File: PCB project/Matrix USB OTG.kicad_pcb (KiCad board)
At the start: 2 copper layers, 27.5 x 20.2 mm, 2 parts, among them J1 USB3150-30-130-A, J2 SSM-102-L-DV

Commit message: Final schematic and initial constraints
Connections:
- J2 pad 01: /USB_DN -> /USB_DP
- J2 pad 02: VBUS -> /USB_DN
- J2 pad 03: /USB_DP -> GND
- J2 pad 04: GND -> VBUS
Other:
- board size 27.5 x 20.2 mm -> 29.2 x 19.5 mm
- board text added: "DN"
- board text added: "DP"
- board text added: "GND"
- board text added: "VBUS"
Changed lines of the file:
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@@
 	)
 	(setup
+		(stackup
+			(layer "F.SilkS"
+				(type "Top Silk Screen")
+			)
+			(layer "F.Paste"
+				(type "Top Solder Paste")
+			)
+			(layer "F.Mask"
+				(type "Top Solder Mask")
+				(thickness 0.01)
+			)
+			(layer "F.Cu"
+				(type "copper")
+				(thickness 0.035)
+			)
+			(layer "dielectric 1"
+				(type "core")
+				(thickness 1.51)
+				(material "FR4")
+				(epsilon_r 4.5)
+				(loss_tangent 0.02)
+			)
+			(layer "B.Cu"
+				(type "copper")
+				(thickness 0.035)
+			)
+			(layer "B.Mask"
+				(type "Bottom Solder Mask")
+				(thickness 0.01)
+			)
+			(layer "B.Paste"
+				(type "Bottom Solder Paste")
+			)
+			(layer "B.SilkS"
+				(type "Bottom Silk Screen")
+			)
+			(copper_finish "None")
+			(dielectric_constraints no)
+		)
 		(pad_to_mask_clearance 0)
 		(allow_soldermask_bridges_in_footprints no)
@@
 		(capping no)
 		(filling no)
+		(zone_defaults)
 		(pcbplotparams
 			(layerselection 0x00000000_00000000_55555555_5755f5ff)
@@
 		(at 107.75 98.5 90)
 		(property "Reference" "J2"
-			(at -0.365 -5.82 90)
+			(at 1.75 8.5 180)
 			(layer "F.SilkS")
 			(effects
@@
 			(size 1.02 2.22)
 			(layers "F.Cu" "F.Mask" "F.Paste")
-			(net "/USB_DN")
+			(net "/USB_DP")
 			(pinfunction "01_01")
 			(pintype "passive")
@@
 			(size 1.02 2.22)
 			(layers "F.Cu" "F.Mask" "F.Paste")
-			(net "VBUS")
+			(net "/USB_DN")
 			(pinfunction "02_02")
 			(pintype "passive")
@@
 			(size 1.02 2.22)
 			(layers "F.Cu" "F.Mask" "F.Paste")
-			(net "/USB_DP")
+			(net "GND")
 			(pinfunction "03_03")
 			(pintype "passive")
@@
 			(size 1.02 2.22)
 			(layers "F.Cu" "F.Mask" "F.Paste")
-			(net "GND")
+			(net "VBUS")
 			(pinfunction "04_04")
 			(pintype "passive")
@@
 		(pad "1" thru_hole circle
 			(at 0 0 180)
-			(size 0.8128 0.8128)
+			(size 0.7628 0.7128)
 			(drill 0.4572)
 			(layers "*.Cu" "*.Mask")
@@
 		(pad "2" thru_hole circle
 			(at 0.650001 0.65 180)
-			(size 0.8128 0.8128)
+			(size 0.7628 0.7628)
 			(drill 0.4572)
 			(layers "*.Cu" "*.Mask")
@@
 		(pad "3" thru_hole circle
 			(at 1.3 0 180)
-			(size 0.8128 0.8128)
+			(size 0.7628 0.7628)
 			(drill 0.4572)
 			(layers "*.Cu" "*.Mask")
@@
 		(pad "4" thru_hole circle
 			(at 1.949999 0.65 180)
-			(size 0.8128 0.8128)
+			(size 0.7628 0.7128)
 			(drill 0.4572)
 			(layers "*.Cu" "*.Mask")
@@
 		(pad "5" thru_hole circle
 			(at 2.6 0 180)
-			(size 0.8128 0.8128)
+			(size 0.7628 0.7128)
 			(drill 0.4572)
 			(layers "*.Cu" "*.Mask")
@@
 		(pad "6" thru_hole circle
 			(at -0.2 1.580001 180)
-			(size 0.8636 0.8636)
+			(size 0.7636 0.7636)
 			(drill 0.5588)
 			(layers "*.Cu" "*.Mask")
@@
 		(pad "7" thru_hole circle
 			(at 2.799999 1.580001 180)
-			(size 0.8636 0.8636)
+			(size 0.7636 0.7636)
 			(drill 0.5588)
 			(layers "*.Cu" "*.Mask")
@@
 		(pad "8" thru_hole circle
 			(at -0.2 -0.919999 180)
-			(size 0.8636 0.8636)
+			(size 0.7636 0.7636)
 			(drill 0.5588)
 			(layers "*.Cu" "*.Mask")
@@
 			(pinfunction "GND_8")
 			(pintype "power_in")
+			(clearance 0)
 		)
 		(pad "9" thru_hole circle
 			(at 2.799999 -0.919999 180)
-			(size 0.8636 0.8636)
+			(size 0.7636 0.7636)
 			(drill 0.5588)
 			(layers "*.Cu" "*.Mask")
@@
 	)
 	(gr_rect
-		(start 102.5 95)
+		(start 100.75 95.75)
 		(end 130 115.25)
 		(stroke
@@
 		(layer "Edge.Cuts")
 	)
+	(gr_text "DN"
+		(at 101.25 98 0)
+		(layer "F.SilkS")
+		(effects
+			(font
+				(size 1 1)
+				(thickness 0.15)
+			)
+			(justify left bottom)
+		)
+	)
+	(gr_text "VBUS"
+		(at 103 102.75 0)
+		(layer "F.SilkS")
+		(effects
+			(font
+				(size 1 1)
+				(thickness 0.15)
+			)
+			(justify left bottom)
+		)
+	)
+	(gr_text "GND"
+		(at 109 102.75 0)
+		(layer "F.SilkS")
+		(effects
+			(font
+				(size 1 1)
+				(thickness 0.15)
+			)
+			(justify left bottom)
+		)
+	)
+	(gr_text "DP"
+		(at 112.75 97.75 0)
+		(layer "F.SilkS")
+		(effects
+			(font
+				(size 1 1)
+				(thickness 0.15)
+			)
+			(justify left bottom)
+		)
+	)
 	(embedded_fonts no)

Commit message: Final shape before review
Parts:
- moved J2 6.03 mm to (113.7, 97.9)
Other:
- board size 29.2 x 19.5 mm -> 20.2 x 19 mm
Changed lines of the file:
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@@
 		(capping no)
 		(filling no)
-		(zone_defaults)
 		(pcbplotparams
 			(layerselection 0x00000000_00000000_55555555_5755f5ff)
@@
 	(footprint "Matrix-USB-OTG:SAMTEC_SSM-102-L-DV"
 		(layer "F.Cu")
-		(at 107.75 98.5 90)
+		(at 113.749999 97.899999 90)
 		(property "Reference" "J2"
-			(at 1.75 8.5 180)
+			(at 0.149999 5.240001 180)
 			(layer "F.SilkS")
 			(effects
@@
 		)
 		(property "Value" "SSM-102-L-DV"
-			(at 8.525 5.8 90)
+			(at -5.650001 -5.069999 90)
 			(layer "F.Fab")
 			(effects
@@
 		(sheetname "/")
 		(sheetfile "Matrix USB OTG.kicad_sch")
-		(units
-			(unit
-				(name "A")
-				(pins "01" "03" "02" "04")
-			)
-		)
 		(attr smd)
 		(duplicate_pad_numbers_are_jumpers no)
 		(fp_line
-			(start 2.54 -2.54)
-			(end 2.54 2.54)
-			(stroke
-				(width 0.2)
-				(type solid)
-			)
-			(layer "F.SilkS")
-		)
-		(fp_line
-			(start 2.13 -2.54)
-			(end 2.54 -2.54)
-			(stroke
-				(width 0.2)
-				(type solid)
-			)
-			(layer "F.SilkS")
-		)
-		(fp_line
 			(start -2.54 -2.54)
 			(end -2.13 -2.54)
-			(stroke
-				(width 0.2)
-				(type solid)
-			)
-			(layer "F.SilkS")
-		)
-		(fp_line
-			(start 2.13 2.54)
-			(end 2.54 2.54)
 			(stroke
 				(width 0.2)
@@
 		(tags "USB3150-30-130-A ")
 		(property "Reference" "J1"
-			(at 1.3 0.65 180)
+			(at -3.910001 1.690001 0)
 			(unlocked yes)
 			(layer "F.SilkS")
@@
 		)
 		(property "Value" "USB3150-30-130-A"
-			(at 1.3 0.65 180)
+			(at 3.959999 3.310001 0)
 			(unlocked yes)
 			(layer "F.Fab")
@@
 		)
 	)
-	(gr_rect
-		(start 100.75 95.75)
-		(end 130 115.25)
-		(stroke
-			(width 0.05)
-			(type default)
-		)
-		(fill no)
+	(gr_arc
+		(start 107.7 97.75)
+		(mid 108.285786 96.335786)
+		(end 109.7 95.75)
+		(stroke
+			(width 0.05)
+			(type default)
+		)
+		(layer "Edge.Cuts")
+	)
+	(gr_line
+		(start 107.7 107.93)
+		(end 107.7 97.75)
+		(stroke
+			(width 0.05)
+			(type default)
+		)
+		(layer "Edge.Cuts")
+	)
+	(gr_arc
+		(start 107.7 107.93)
+		(mid 112.501255 109.918745)
+		(end 114.49 114.72)
+		(stroke
+			(width 0.05)
+			(type default)
+		)
+		(layer "Edge.Cuts")
+	)
+	(gr_line
+		(start 109.7 95.75)
+		(end 118.01 95.75)
+		(stroke
+			(width 0.05)
+			(type default)
+		)
+		(layer "Edge.Cuts")
+	)
+	(gr_line
+		(start 114.49 114.72)
+		(end 125.9 114.72)
+		(stroke
+			(width 0.05)
+			(type default)
+		)
+		(layer "Edge.Cuts")
+	)
+	(gr_arc
+		(start 118.01 95.75)
+		(mid 119.424214 96.335786)
+		(end 120.01 97.75)
+		(stroke
+			(width 0.05)
+			(type default)
+		)
+		(layer "Edge.Cuts")
+	)
+	(gr_line
+		(start 120.01 97.74)
+		(end 120.01 105.65)
+		(stroke
+			(width 0.05)
+			(type default)
+		)
+		(layer "Edge.Cuts")
+	)
+	(gr_arc
+		(start 122.01 107.65)
+		(mid 120.595786 107.064214)
+		(end 120.01 105.65)
+		(stroke
+			(width 0.05)
+			(type default)
+		)
+		(layer "Edge.Cuts")
+	)
+	(gr_line
+		(start 125.9 107.644214)
+		(end 122.01 107.644214)
+		(stroke
+			(width 0.05)
+			(type default)
+		)
+		(layer "Edge.Cuts")
+	)
+	(gr_arc
+		(start 125.9 107.644214)
+		(mid 127.314214 108.23)
+		(end 127.9 109.644214)
+		(stroke
+			(width 0.05)
+			(type default)
+		)
+		(layer "Edge.Cuts")
+	)
+	(gr_line
+		(start 127.9 109.644214)
+		(end 127.9 112.72)
+		(stroke
+			(width 0.05)
+			(type default)
+		)
+		(layer "Edge.Cuts")
+	)
+	(gr_arc
+		(start 127.9 112.72)
+		(mid 127.314214 114.134214)
+		(end 125.9 114.72)
+		(stroke
+			(width 0.05)
+			(type default)
+		)
 		(layer "Edge.Cuts")
 	)
 	(gr_text "DN"
-		(at 101.25 98 0)
+		(at 109.8 102.2 0)
 		(layer "F.SilkS")
 		(effects
@@
 	)
 	(gr_text "VBUS"
-		(at 103 102.75 0)
+		(at 110.1 104 0)
 		(layer "F.SilkS")
 		(effects
@@
 	)
 	(gr_text "GND"
-		(at 109 102.75 0)
+		(at 115 104 0)
 		(layer "F.SilkS")
 		(effects
@@
 	)
 	(gr_text "DP"
-		(at 112.75 97.75 0)
+		(at 115.1 102.4 0)
 		(layer "F.SilkS")
 		(effects

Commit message: Firs routing approach
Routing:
- net /USB_DP: track 0.00 -> 25.4 mm, vias 0 -> 1
- net /USB_DN: track 0.00 -> 24.5 mm, vias 0 -> 1
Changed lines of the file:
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@@
 			(layers)
 		)
-		(pad "1" thru_hole circle
+		(pad "1" thru_hole oval
 			(at 0 0 180)
-			(size 0.7628 0.7128)
+			(size 0.6 0.8)
 			(drill 0.4572)
 			(layers "*.Cu" "*.Mask")
@@
 			(pinfunction "VBUS_1")
 			(pintype "power_in")
-		)
-		(pad "2" thru_hole circle
+			(thermal_bridge_angle 45)
+		)
+		(pad "2" thru_hole oval
 			(at 0.650001 0.65 180)
-			(size 0.7628 0.7628)
+			(size 0.6 0.8)
 			(drill 0.4572)
 			(layers "*.Cu" "*.Mask")
@@
 			(pinfunction "D-_2")
 			(pintype "bidirectional")
-		)
-		(pad "3" thru_hole circle
+			(thermal_bridge_angle 45)
+		)
+		(pad "3" thru_hole oval
 			(at 1.3 0 180)
-			(size 0.7628 0.7628)
+			(size 0.6 0.8)
 			(drill 0.4572)
 			(layers "*.Cu" "*.Mask")
@@
 			(pintype "bidirectional")
 		)
-		(pad "4" thru_hole circle
+		(pad "4" thru_hole oval
 			(at 1.949999 0.65 180)
-			(size 0.7628 0.7128)
+			(size 0.6 0.8)
 			(drill 0.4572)
 			(layers "*.Cu" "*.Mask")
@@
 		)
 	)
+	(segment
+		(start 113.802 104.017742)
+		(end 118.883258 109.099)
+		(width 0.25)
+		(layer "F.Cu")
+		(net "/USB_DP")
+	)
+	(segment
+		(start 116.574999 96.629999)
+		(end 114.570001 96.629999)
+		(width 0.25)
+		(layer "F.Cu")
+		(net "/USB_DP")
+	)
+	(segment
+		(start 114.570001 96.629999)
+		(end 113.802 97.398)
+		(width 0.25)
+		(layer "F.Cu")
+		(net "/USB_DP")
+	)
+	(segment
+		(start 113.802 97.398)
+		(end 113.802 104.017742)
+		(width 0.25)
+		(layer "F.Cu")
+		(net "/USB_DP")
+	)
+	(segment
+		(start 118.883258 109.099)
+		(end 122.825 109.099)
+		(width 0.25)
+		(layer "F.Cu")
+		(net "/USB_DP")
+	)
+	(segment
+		(start 122.825 109.099)
+		(end 123 108.924)
+		(width 0.25)
+		(layer "F.Cu")
+		(net "/USB_DP")
+	)
+	(via
+		(at 123 108.924)
+		(size 0.6)
+		(drill 0.3)
+		(layers "F.Cu" "B.Cu")
+		(net "/USB_DP")
+	)
+	(segment
+		(start 122.825 109.099)
+		(end 122.416742 109.099)
+		(width 0.25)
+		(layer "B.Cu")
+		(net "/USB_DP")
+	)
+	(segment
+		(start 121.491012 111.539529)
+		(end 121.549999 111.598516)
+		(width 0.25)
+		(layer "B.Cu")
+		(net "/USB_DP")
+	)
+	(segment
+		(start 122.416742 109.099)
+		(end 121.491012 110.024732)
+		(width 0.25)
+		(layer "B.Cu")
+		(net "/USB_DP")
+	)
+	(segment
+		(start 121.549999 111.598516)
+		(end 121.549999 112.330001)
+		(width 0.25)
+		(layer "B.Cu")
+		(net "/USB_DP")
+	)
+	(segment
+		(start 121.491012 110.024732)
+		(end 121.491012 111.539529)
+		(width 0.25)
+		(layer "B.Cu")
+		(net "/USB_DP")
+	)
+	(segment
+		(start 123 108.924)
+		(end 122.825 109.099)
+		(width 0.25)
+		(layer "B.Cu")
+		(net "/USB_DP")
+	)
+	(segment
+		(start 112.629999 96.629999)
+		(end 113.4 97.4)
+		(width 0.25)
+		(layer "F.Cu")
+		(net "/USB_DN")
+	)
+	(segment
+		(start 110.924999 96.629999)
+		(end 112.629999 96.629999)
+		(width 0.25)
+		(layer "F.Cu")
+		(net "/USB_DN")
+	)
+	(segment
+		(start 122.825 109.501)
+		(end 123 109.676)
+		(width 0.25)
+		(layer "F.Cu")
+		(net "/USB_DN")
+	)
+	(segment
+		(start 113.4 104.184256)
+		(end 118.716744 109.501)
+		(width 0.25)
+		(layer "F.Cu")
+		(net "/USB_DN")
+	)
+	(segment
+		(start 118.716744 109.501)
+		(end 122.825 109.501)
+		(width 0.25)
+		(layer "F.Cu")
+		(net "/USB_DN")
+	)
+	(segment
+		(start 113.4 97.4)
+		(end 113.4 104.184256)
+		(width 0.25)
+		(layer "F.Cu")
+		(net "/USB_DN")
+	)
+	(via
+		(at 123 109.676)
+		(size 0.6)
+		(drill 0.3)
+		(layers "F.Cu" "B.Cu")
+		(net "/USB_DN")
+	)
+	(segment
+		(start 122.583258 109.501)
+		(end 121.893012 110.191246)
+		(width 0.25)
+		(layer "B.Cu")
+		(net "/USB_DN")
+	)
+	(segment
+		(start 121.893012 110.191246)
+		(end 121.893012 111.373015)
+		(width 0.25)
+		(layer "B.Cu")
+		(net "/USB_DN")
+	)
+	(segment
+		(start 121.893012 111.373015)
+		(end 122.199998 111.680001)
+		(width 0.25)
+		(layer "B.Cu")
+		(net "/USB_DN")
+	)
+	(segment
+		(start 123 109.676)
+		(end 122.825 109.501)
+		(width 0.25)
+		(layer "B.Cu")
+		(net "/USB_DN")
+	)
+	(segment
+		(start 122.825 109.501)
+		(end 122.583258 109.501)
+		(width 0.25)
+		(layer "B.Cu")
+		(net "/USB_DN")
+	)
 	(embedded_fonts no)

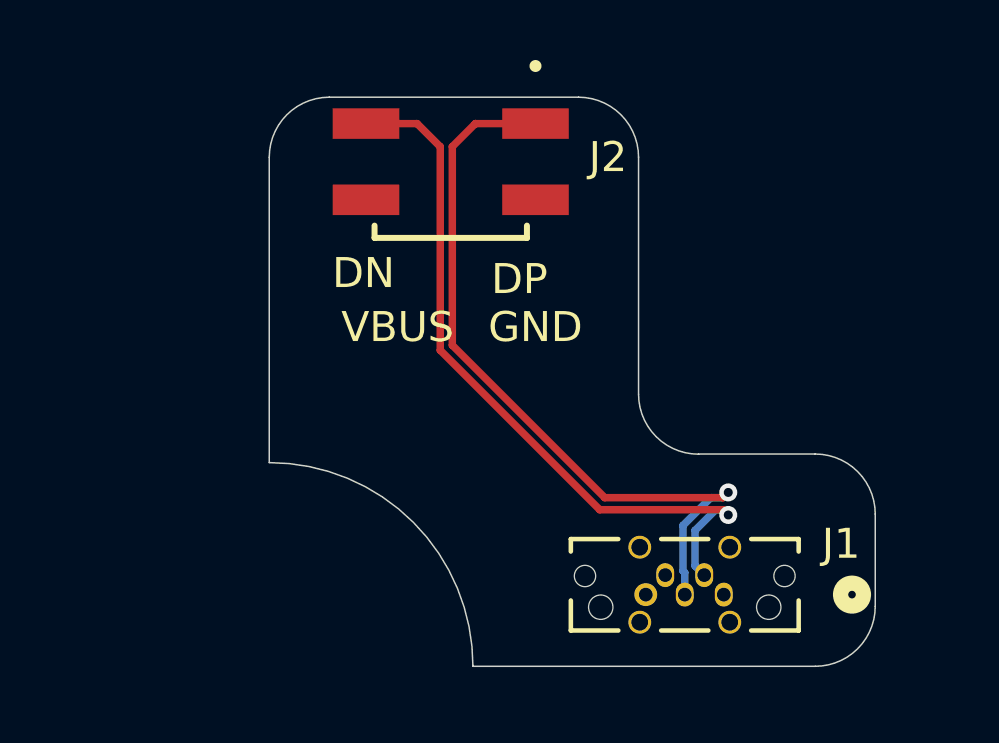
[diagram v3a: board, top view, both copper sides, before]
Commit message: Make the PCB smaller so it can work with ESQ-105-23-T-D
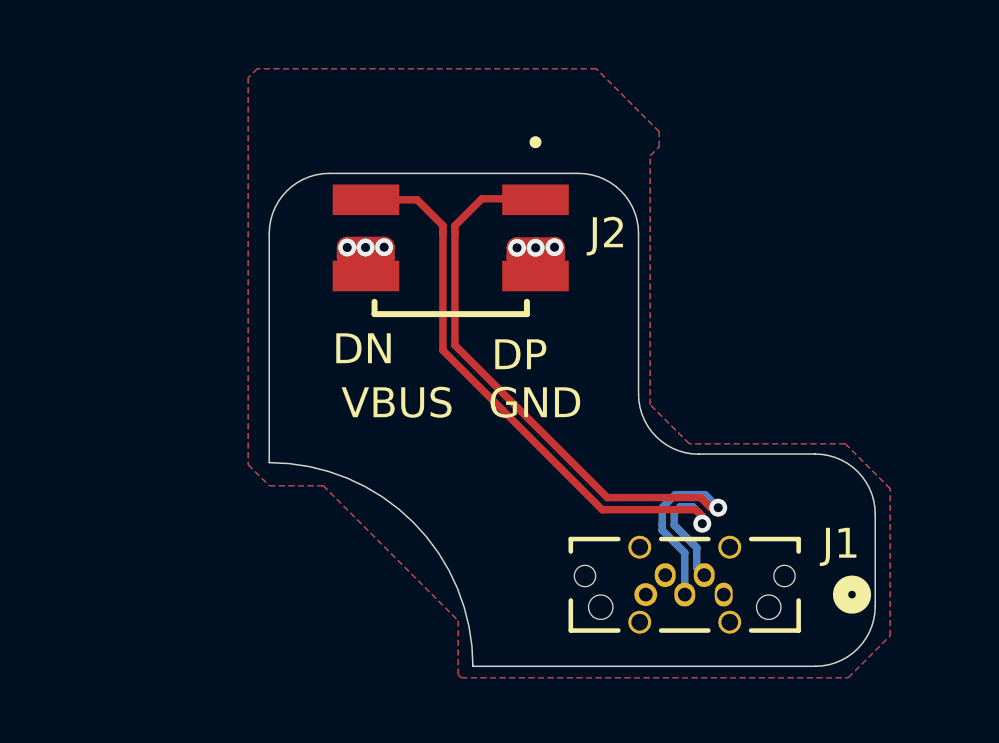
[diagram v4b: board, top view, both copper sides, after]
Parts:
- moved J2 2.54 mm to (113.7, 100.4)
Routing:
- net VBUS: track 0.00 -> 4.71 mm, vias 0 -> 3
- net GND: track 0.00 -> 4.65 mm, vias 0 -> 3
- net /USB_DN: track 24.5 -> 22.2 mm
- net /USB_DP: track 25.4 -> 23.4 mm
- added copper zone on F.Cu, net GND
- added copper zone on In1.Cu, net GND
- added copper zone on In2.Cu, net GND
- added copper zone on B.Cu, net VBUS
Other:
- board size 20.2 x 19 mm -> 20.2 x 16.4 mm
- copper layers 2 -> 4

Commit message: Fix USB footprint issues and change the pcb width to 0.8mm as per USB 3150 datasheet
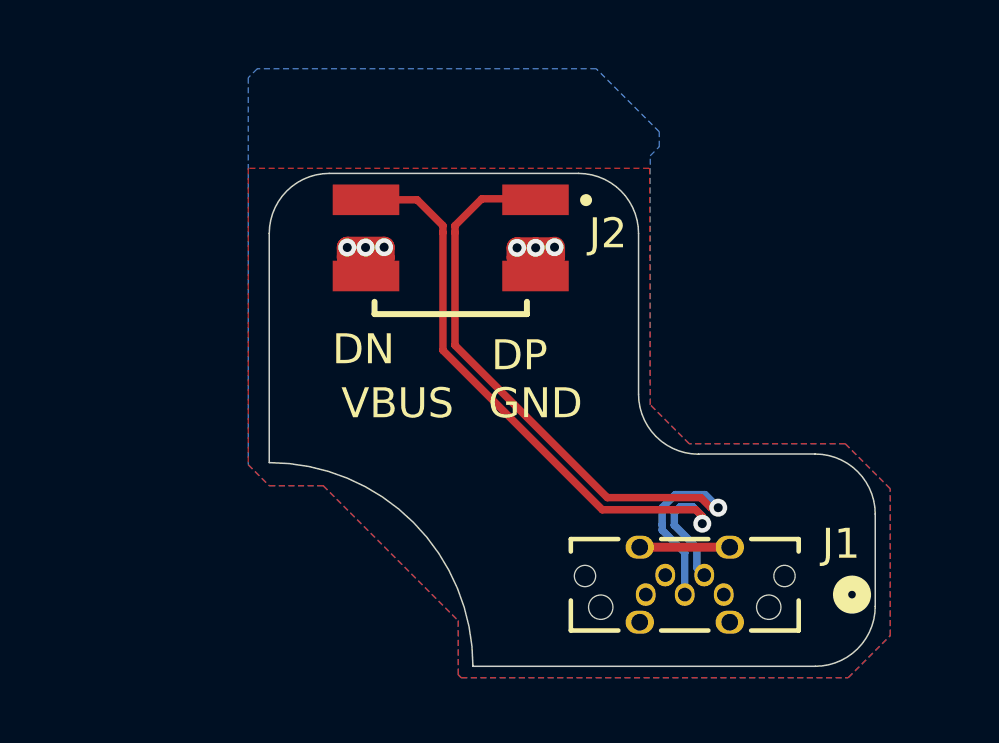
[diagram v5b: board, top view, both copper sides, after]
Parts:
- J1: value USB3150-30-130-A -> USB3150-30-70-A
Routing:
- net GND: track 4.65 -> 7.65 mm

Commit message: Design is ready to create Manufacturing files, check BoM
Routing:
- net GND: track 7.65 -> 3.00 mm, vias 3 -> 4
- net VBUS: track 4.71 -> 5.06 mm, vias 3 -> 4
